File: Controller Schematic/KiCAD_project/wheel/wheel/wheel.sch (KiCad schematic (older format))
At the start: 56 parts, among them J4 Conn_02x13_Top_Bottom, U3 4N35

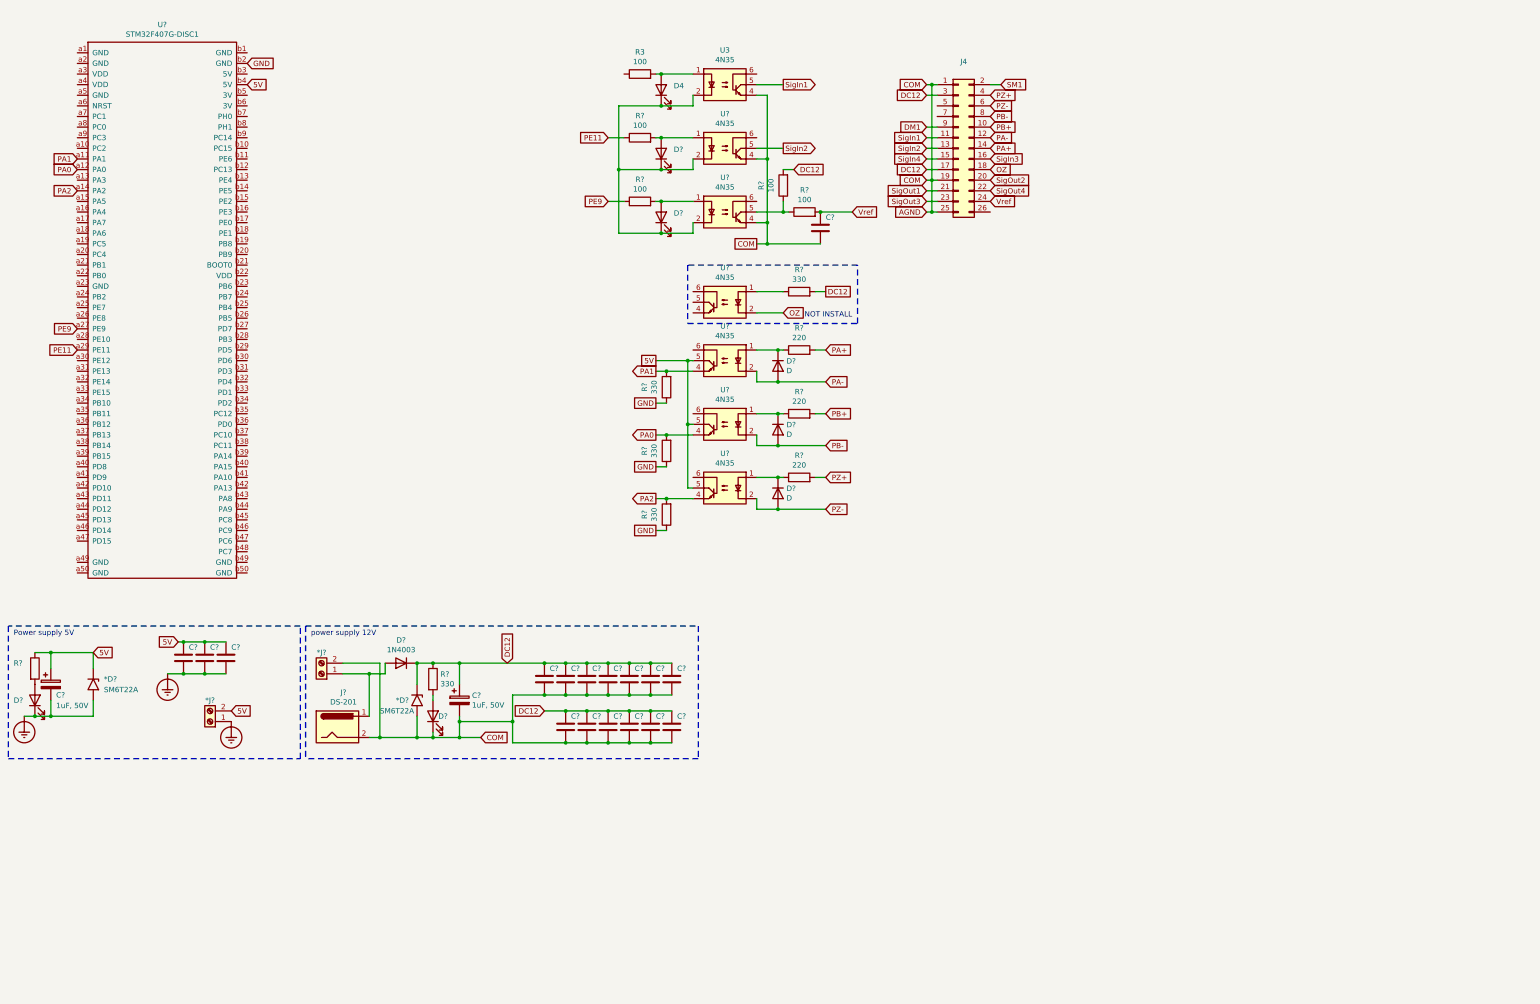
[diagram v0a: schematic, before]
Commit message: Wheel's PCB changed
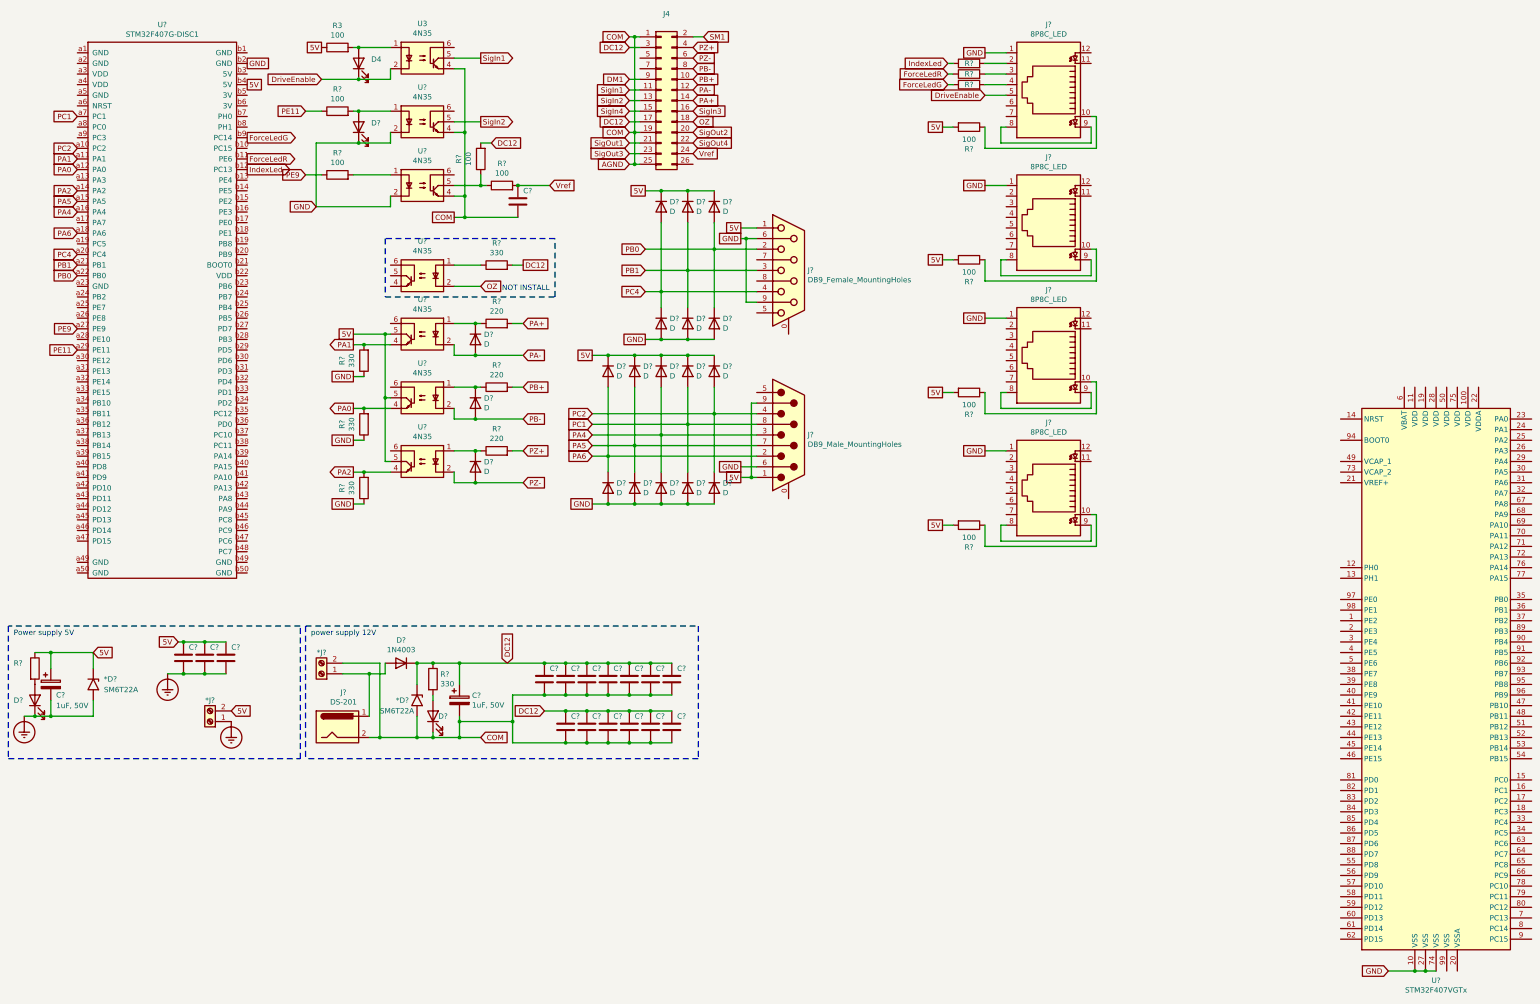
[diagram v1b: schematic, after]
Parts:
- removed D?: BL-LS0805UYC, LED_SMD:LED_0805_2012Metric, symbol Device:LED
- added D? (x16): D, symbol Device:D
- added J? (x4): 8P8C_LED, symbol Connector:8P8C_LED
- added J?: DB9_Female_MountingHoles, symbol Connector:DB9_Female_MountingHoles
- added J?: DB9_Male_MountingHoles, symbol Connector:DB9_Male_MountingHoles
- added R? (x4): 100, Resistor_SMD:R_0805_2012Metric, symbol Device:R
- added R? (x3): 220, Resistor_SMD:R_0805_2012Metric, symbol Device:R
- added U?: STM32F407VGTx, Package_QFP:LQFP-100_14x14mm_P0.5mm, symbol MCU_ST_STM32F4:STM32F407VGTx
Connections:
- net 5V: now also R3.1, D?.1 (K), D?.1 (K), D?.1 (K), D?.1 (K), D?.1 (K), D?.1 (K), D?.1 (K), D?.1 (K), J?.1, J?.1, J?.9, R?.2, R?.2, R?.2, R?.2
- net GND: now also D?.1 (K), U?.2, U?.2, D?.2 (A), D?.2 (A), D?.2 (A), D?.2 (A), D?.2 (A), D?.2 (A), D?.2 (A), D?.2 (A), J?.1, J?.1, J?.1, J?.1, J?.6, J?.6, J?.9, U?.10 (VSS), U?.27 (VSS), U?.74 (VSS)
- net PC2: now reaches U?.a10 (PC2)
- net PC2: now also D?.1 (K), D?.2 (A), J?.4
- net PA5: now reaches U?.a15 (PA5)
- net PA5: now also D?.1 (K), D?.2 (A), J?.7
- net PA4: now reaches U?.a16 (PA4)
- net PA4: now also D?.1 (K), D?.2 (A), J?.3
- net PA6: now reaches U?.a18 (PA6)
- net PA6: now also D?.1 (K), D?.2 (A), J?.2
- net PC4: now reaches U?.a20 (PC4)
- net PC4: now also D?.1 (K), D?.2 (A), J?.4
- net PB1: now reaches U?.a21 (PB1)
- net PB1: now also D?.1 (K), D?.2 (A), J?.3
- net PB0: now reaches U?.a22 (PB0)
- net PB0: now also D?.1 (K), D?.2 (A), J?.2
- net PC1: now reaches U?.a7 (PC1)
- net PC1: now also D?.1 (K), D?.2 (A), J?.8
- net ForceLedR: now reaches U?.b11 (PE6)
- net ForceLedR: now also R?.1
- net IndexLed: now reaches U?.b12 (PC13)
- net IndexLed: now also R?.1
- net ForceLedG: now reaches U?.b9 (PC14)
- net ForceLedG: now also R?.1
- new net: J?.10, R?.1 (x4)
- new net: J?.2, R?.2
- new net: J?.3, R?.2
- new net: J?.4, R?.2
- new net: J?.8, J?.9 (x4)
- new net DriveEnable: D4.1 (K), J?.5, U3.2
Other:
- moved on the sheet: C?, D4, D?, J4, R3, R?, U3, U?
